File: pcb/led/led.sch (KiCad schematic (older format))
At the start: 6 parts, among them J1 RJ45, Q1 BC849

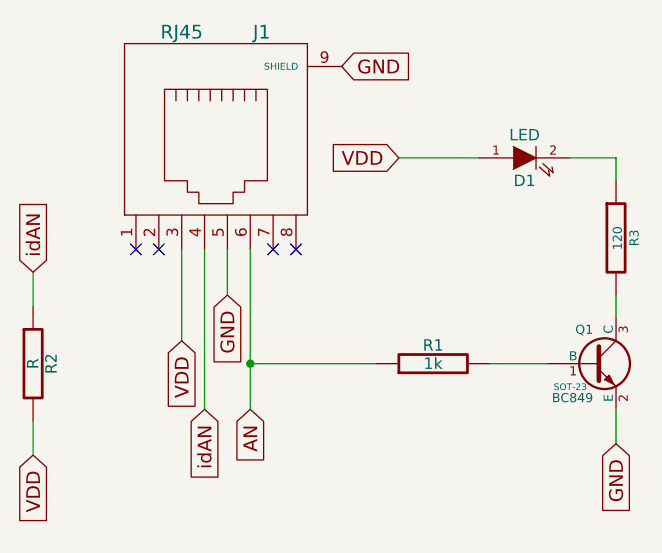
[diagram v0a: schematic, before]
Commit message: new module led and somes changes
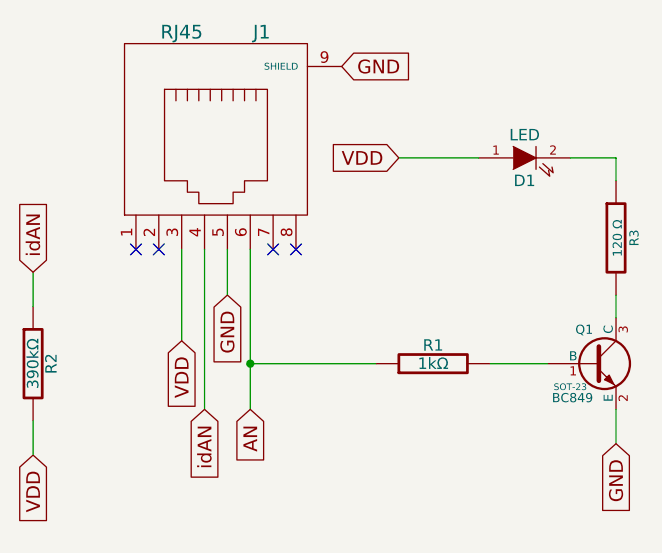
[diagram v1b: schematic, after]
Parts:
- R1: value 1k -> 1kΩ
- R2: value R -> 390kΩ
- R3: value 120 -> 120 Ω
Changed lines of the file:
@@
-EESchema Schematic File Version 2  date jue 21 mar 2013 10:20:34 UYT
+EESchema Schematic File Version 2  date vie 03 may 2013 14:35:26 UYT
 LIBS:power
 LIBS:device
@@
 LIBS:contrib
 LIBS:valves
-EELAYER 27 0
+LIBS:led-cache
+EELAYER 25  0
 EELAYER END
-$Descr A4 11693 8268
+$Descr A4 11700 8267
 encoding utf-8
 Sheet 1 1
 Title ""
-Date "21 mar 2013"
+Date "3 may 2013"
 Rev ""
 Comp ""
@@
 P 1550 2450
 F 0 "R2" V 1630 2450 50  0000 C CNN
-F 1 "R" V 1550 2450 50  0000 C CNN
-F 2 "" H 1550 2450 60  0001 C CNN
-F 3 "" H 1550 2450 60  0001 C CNN
+F 1 "390kΩ" V 1550 2450 50  0000 C CNN
 	1    1550 2450
 	1    0    0    -1
@@
 F 0 "J1" H 2550 2000 60  0000 C CNN
 F 1 "RJ45" H 2200 2000 60  0000 C CNN
-F 2 "" H 2350 1500 60  0001 C CNN
-F 3 "" H 2350 1500 60  0001 C CNN
 	1    2350 1500
 	1    0    0    -1
@@
 P 3300 2450
 F 0 "R1" V 3380 2450 50  0000 C CNN
-F 1 "1k" V 3300 2450 50  0000 C CNN
-F 2 "" H 3300 2450 60  0001 C CNN
-F 3 "" H 3300 2450 60  0001 C CNN
+F 1 "1kΩ" V 3300 2450 50  0000 C CNN
 	1    3300 2450
 	0    -1   -1   0
@@
 P 4100 1900
 F 0 "R3" V 4180 1900 40  0000 C CNN
-F 1 "120" V 4107 1899 40  0000 C CNN
+F 1 "120 Ω" V 4107 1899 40  0000 C CNN
 F 2 "~" V 4030 1900 30  0000 C CNN
 F 3 "~" H 4100 1900 30  0000 C CNN
